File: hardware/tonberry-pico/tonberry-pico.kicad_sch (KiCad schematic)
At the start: 10 parts, among them J1 MicroSD_Breakout, J2 SparkFun I2S Audio Breakout M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, J3 RC522_Breakout, SW1 SW_Push, SW2 SW_Push, SW3 SW_Push, U1 Pico

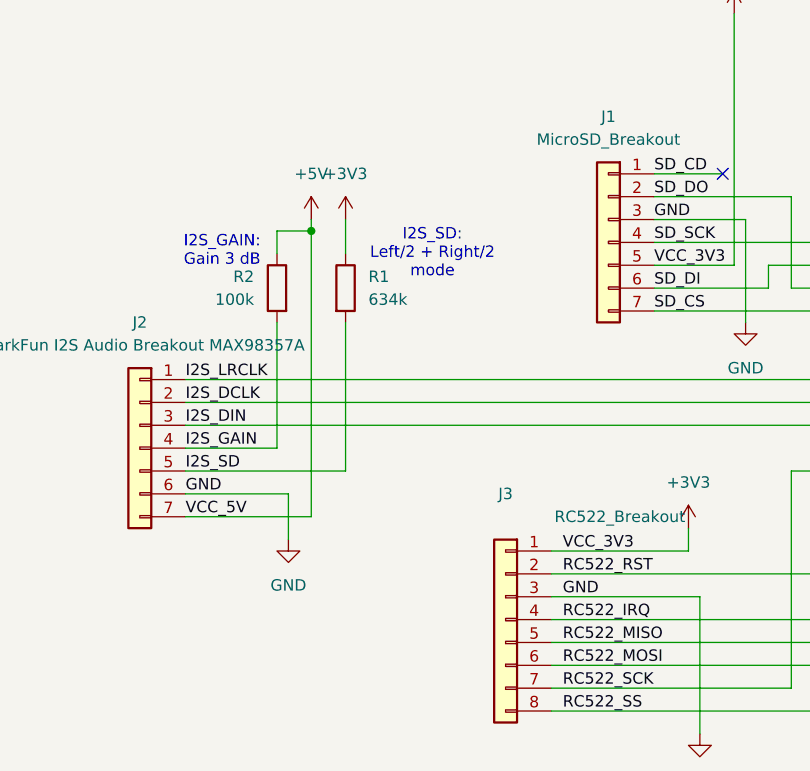
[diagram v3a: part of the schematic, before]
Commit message: schematic: Fix I2S_SD pullup
Sparkfun I2S audio board already has MAX98357A SD pin pullup for mono
mode, so external pullup is redundant and can actually cause issues.
Remove it.
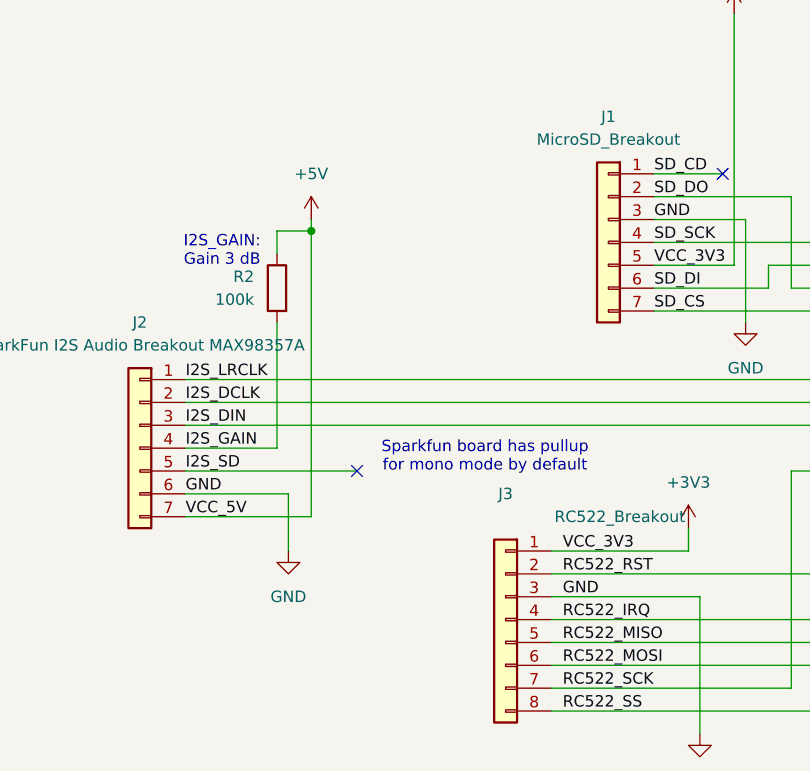
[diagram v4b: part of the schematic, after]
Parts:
- removed R1: 634k, symbol Device:R
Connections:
- no-connect marks 2 -> 3
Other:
- note added: "Sparkfun board has pullup for mono mode by default"
- note removed: "I2S_SD: Left/2 + Right/2 mode"
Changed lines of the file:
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@@
 		)
 	)
-	(text "I2S_SD:\nLeft/2 + Right/2\nmode"
+	(text "Sparkfun board has pullup\nfor mono mode by default"
 		(exclude_from_sim no)
-		(at 59.182 68.58 0)
+		(at 65.024 91.186 0)
 		(effects
 			(font
@@
 	)
 	(no_connect
+		(at 50.8 92.71)
+	)
+	(no_connect
 		(at 170.18 139.7)
 	)
@@
 	(wire
 		(pts
-			(xy 31.75 92.71) (xy 49.53 92.71)
-		)
-		(stroke
-			(width 0)
-			(type default)
-		)
-	)
-	(wire
-		(pts
 			(xy 157.48 59.69) (xy 162.56 59.69)
 		)
@@
 	(wire
 		(pts
+			(xy 31.75 92.71) (xy 50.8 92.71)
+		)
+		(stroke
+			(width 0)
+			(type default)
+		)
+	)
+	(wire
+		(pts
 			(xy 121.92 85.09) (xy 104.14 85.09)
 		)
@@
 	(wire
 		(pts
-			(xy 49.53 76.2) (xy 49.53 92.71)
-		)
-		(stroke
-			(width 0)
-			(type default)
-		)
-	)
-	(wire
-		(pts
 			(xy 99.06 62.23) (xy 99.06 72.39)
 		)
@@
 	(wire
 		(pts
-			(xy 43.18 100.33) (xy 43.18 95.25)
+			(xy 43.18 95.25) (xy 43.18 101.6)
 		)
 		(stroke
@@
 		(pts
 			(xy 72.39 104.14) (xy 109.22 104.14)
-		)
-		(stroke
-			(width 0)
-			(type default)
-		)
-	)
-	(wire
-		(pts
-			(xy 49.53 64.77) (xy 49.53 68.58)
 		)
 		(stroke
@@
 			)
 			(justify left bottom)
-		)
-	)
-	(symbol
-		(lib_id "Device:R")
-		(at 49.53 72.39 0)
-		(unit 1)
-		(exclude_from_sim no)
-		(in_bom yes)
-		(on_board yes)
-		(dnp no)
-		(property "Reference" "R1"
-			(at 52.07 71.1199 0)
-			(effects
-				(font
-					(size 1.27 1.27)
-				)
-				(justify left)
-			)
-		)
-		(property "Value" "634k"
-			(at 52.07 73.6599 0)
-			(effects
-				(font
-					(size 1.27 1.27)
-				)
-				(justify left)
-			)
-		)
-		(property "Footprint" ""
-			(at 47.752 72.39 90)
-			(effects
-				(font
-					(size 1.27 1.27)
-				)
-				(hide yes)
-			)
-		)
-		(property "Datasheet" "~"
-			(at 49.53 72.39 0)
-			(effects
-				(font
-					(size 1.27 1.27)
-				)
-				(hide yes)
-			)
-		)
-		(property "Description" "Resistor"
-			(at 49.53 72.39 0)
-			(effects
-				(font
-					(size 1.27 1.27)
-				)
-				(hide yes)
-			)
-		)
-		(pin "2"
-		)
-		(pin "1"
-		)
-		(instances
-			(project "tonberry-pico"
-				(path "/7226ca0f-138a-46b4-89f3-dc32dfb1f9f7"
-					(reference "R1")
-					(unit 1)
-				)
-			)
-		)
-	)
-	(symbol
-		(lib_id "power:+3V3")
-		(at 49.53 64.77 0)
-		(unit 1)
-		(exclude_from_sim no)
-		(in_bom yes)
-		(on_board yes)
-		(dnp no)
-		(fields_autoplaced yes)
-		(property "Reference" "#PWR07"
-			(at 49.53 68.58 0)
-			(effects
-				(font
-					(size 1.27 1.27)
-				)
-				(hide yes)
-			)
-		)
-		(property "Value" "+3V3"
-			(at 49.53 59.69 0)
-			(effects
-				(font
-					(size 1.27 1.27)
-				)
-			)
-		)
-		(property "Footprint" ""
-			(at 49.53 64.77 0)
-			(effects
-				(font
-					(size 1.27 1.27)
-				)
-				(hide yes)
-			)
-		)
-		(property "Datasheet" ""
-			(at 49.53 64.77 0)
-			(effects
-				(font
-					(size 1.27 1.27)
-				)
-				(hide yes)
-			)
-		)
-		(property "Description" "Power symbol creates a global label with name \"+3V3\""
-			(at 49.53 64.77 0)
-			(effects
-				(font
-					(size 1.27 1.27)
-				)
-				(hide yes)
-			)
-		)
-		(pin "1"
-		)
-		(instances
-			(project "tonberry-pico"
-				(path "/7226ca0f-138a-46b4-89f3-dc32dfb1f9f7"
-					(reference "#PWR07")
-					(unit 1)
-				)
-			)
 		)
 	)
@@
 	(symbol
 		(lib_id "power:GND")
-		(at 43.18 100.33 0)
+		(at 43.18 101.6 0)
 		(unit 1)
 		(exclude_from_sim no)
@@
 		(fields_autoplaced yes)
 		(property "Reference" "#PWR05"
+			(at 43.18 107.95 0)
+			(effects
+				(font
+					(size 1.27 1.27)
+				)
+				(hide yes)
+			)
+		)
+		(property "Value" "GND"
 			(at 43.18 106.68 0)
 			(effects
@@
 					(size 1.27 1.27)
 				)
-				(hide yes)
-			)
-		)
-		(property "Value" "GND"
-			(at 43.18 105.41 0)
-			(effects
-				(font
-					(size 1.27 1.27)
-				)
 			)
 		)
 		(property "Footprint" ""
-			(at 43.18 100.33 0)
+			(at 43.18 101.6 0)
 			(effects
 				(font
@@
 		)
 		(property "Datasheet" ""
-			(at 43.18 100.33 0)
+			(at 43.18 101.6 0)
 			(effects
 				(font
@@
 		)
 		(property "Description" "Power symbol creates a global label with name \"GND\" , ground"
-			(at 43.18 100.33 0)
-			(effects
-				(font
+			(at 43.18 101.6 0)
+			(effects
+				(font

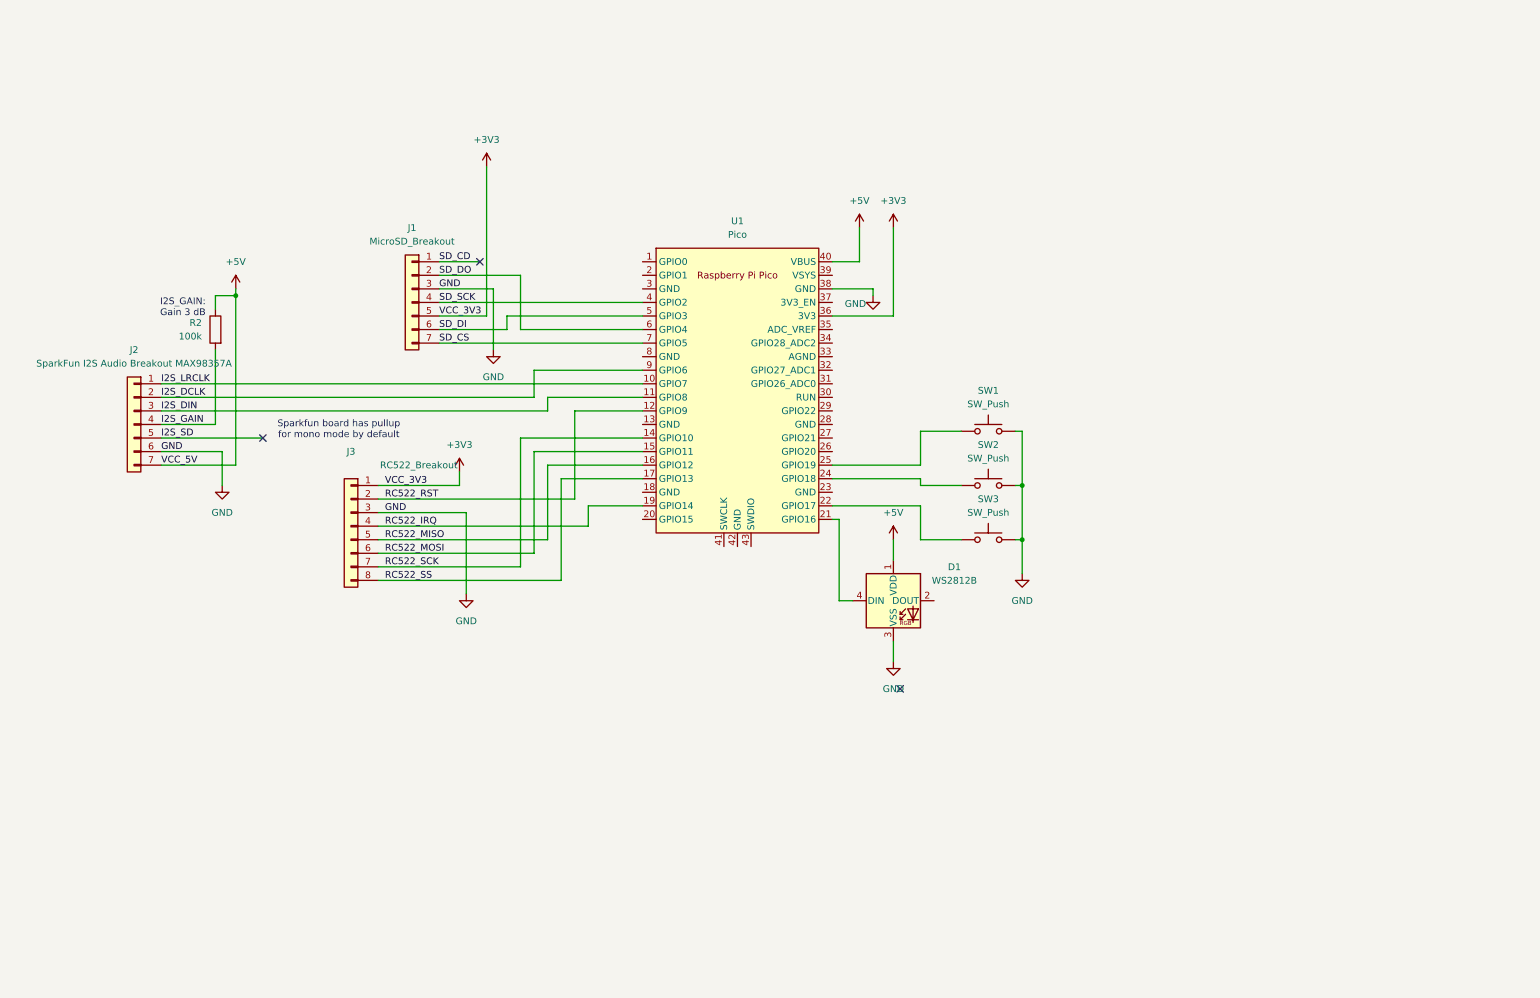
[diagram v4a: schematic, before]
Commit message: Add battery charger, PCB rev 1
Signed-off-by: Matthias Blankertz <matthias@blankertz.org>
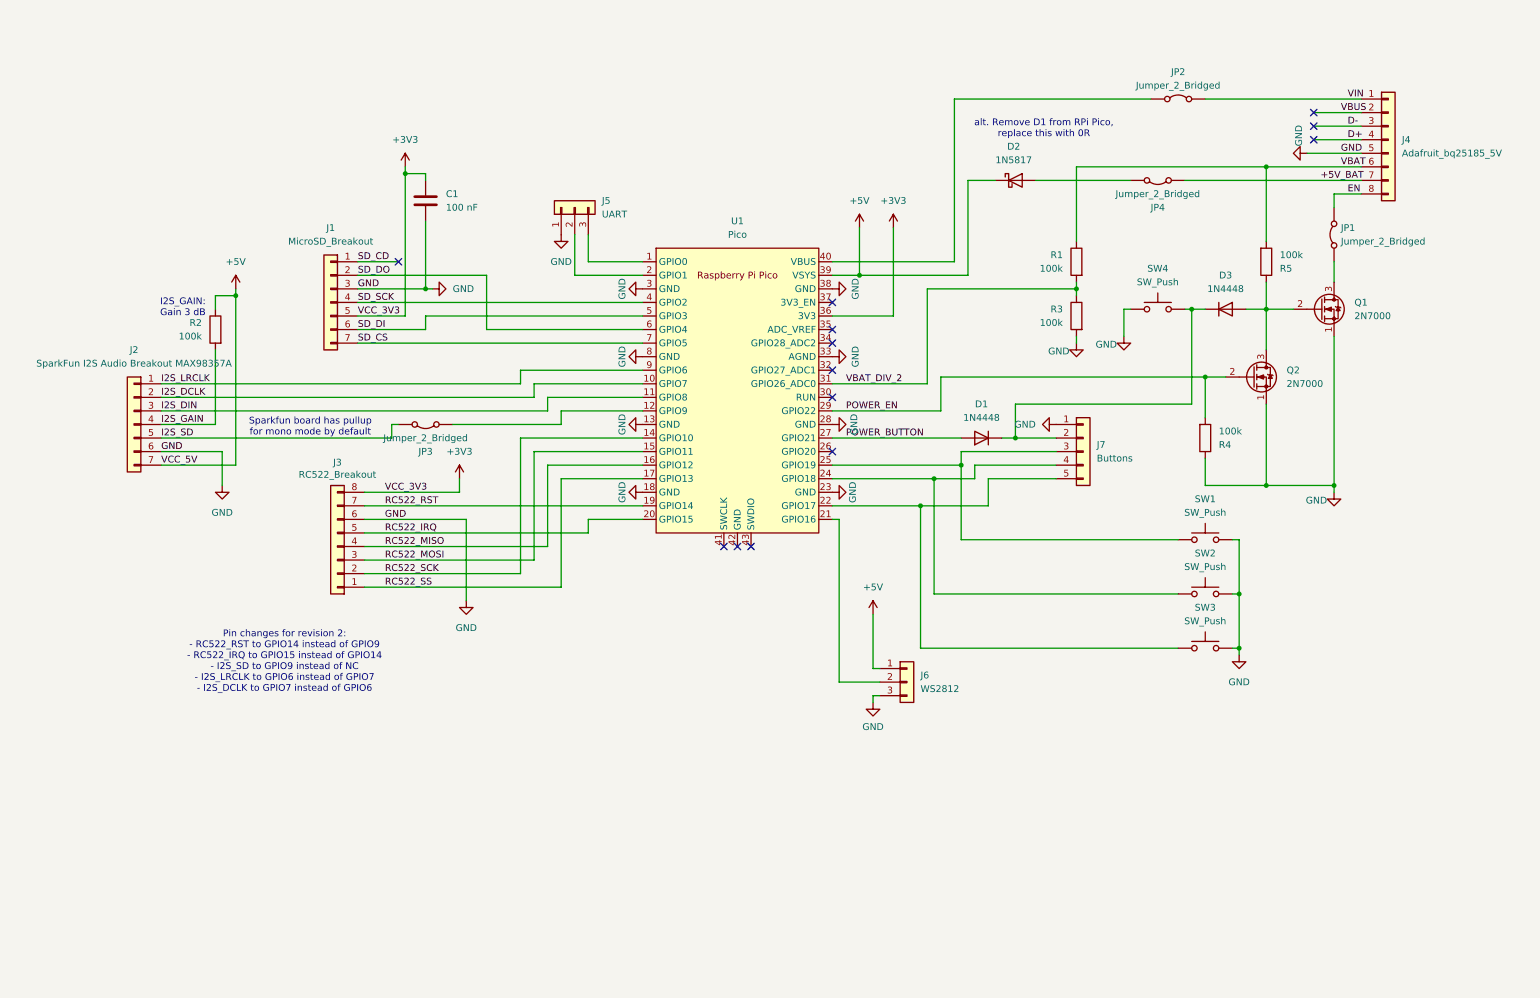
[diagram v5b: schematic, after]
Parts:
- removed D1: WS2812B, LED_SMD:LED_WS2812B_PLCC4_5.0x5.0mm_P3.2mm, symbol LED:WS2812B
- added C1: 100 nF, Capacitor_THT:C_Disc_D5.0mm_W2.5mm_P5.00mm, symbol Device:C
- added D1, D3: 1N4448, Diode_THT:D_DO-35_SOD27_P7.62mm_Horizontal, symbol Device:D
- added D2: 1N5817, Diode_THT:D_DO-41_SOD81_P10.16mm_Horizontal, symbol Device:D_Schottky
- added J4: Adafruit_bq25185_5V, Modules:Adafruit_bq25185, symbol Connector_Generic:Conn_01x08
- added J5: UART, Connector_PinHeader_2.54mm:PinHeader_1x03_P2.54mm_Vertical, symbol Connector_Generic:Conn_01x03
- added J6: WS2812, Connector_PinSocket_2.54mm:PinSocket_1x03_P2.54mm_Vertical, symbol Connector_Generic:Conn_01x03
- added J7: Buttons, Connector_PinSocket_2.54mm:PinSocket_1x05_P2.54mm_Vertical, symbol Connector_Generic:Conn_01x05
- added JP1, JP2, JP3, JP4: Jumper_2_Bridged, Connector_PinHeader_2.54mm:PinHeader_1x02_P2.54mm_Vertical, symbol Jumper:Jumper_2_Bridged
- added Q1, Q2: 2N7000, Package_TO_SOT_THT:TO-92_Inline, symbol Transistor_FET:2N7000
- added R1, R3, R4, R5: 100k, Resistor_THT:R_Axial_DIN0207_L6.3mm_D2.5mm_P10.16mm_Horizontal, symbol Device:R
- added SW4: SW_Push, Button_Switch_THT:Push_E-Switch_KS01Q01, symbol Switch:SW_Push
- J1: footprint (none) -> Modules:Sparkfun_MicroSD_Breakout
- J2: footprint (none) -> Modules:Sparkfun_MAX98357A
- J3: footprint (none) -> Modules:AZ_Delivery_RC522
- R2: footprint (none) -> Resistor_THT:R_Axial_DIN0207_L6.3mm_D2.5mm_P10.16mm_Horizontal
- SW1, SW2, SW3: footprint (none) -> Button_Switch_THT:Push_E-Switch_KS01Q01
- U1: footprint RPi_Pico:RPi_Pico_SMD_TH -> Module:RaspberryPi_Pico_Common_THT
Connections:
- net +3V3: now also J3.8 (Pin_8), C1.1; no longer J3.1 (Pin_1)
- net +5V: now also U1.39 (VSYS), D2.1 (K), J6.1 (Pin_1); no longer U1.40 (VBUS)
- net GND: now also J3.6 (Pin_6), U1.13 (GND), U1.18 (GND), U1.23 (GND), U1.28 (GND), U1.3 (GND), U1.33 (AGND), U1.8 (GND), C1.2, J4.5 (Pin_5), J5.1 (Pin_1), J6.3 (Pin_3), J7.1 (Pin_1), Q1.1 (S), Q2.1 (S), R3.2, R4.1, SW4.2; no longer J3.3 (Pin_3)
- net I2S_DCLK: now also U1.10 (GPIO7); no longer U1.9 (GPIO6)
- net I2S_LRCLK: now also U1.9 (GPIO6); no longer U1.10 (GPIO7)
- net I2S_SD: now also JP3.1 (A)
- net RC522_IRQ: now also J3.5 (Pin_5), U1.20 (GPIO15); no longer J3.4 (Pin_4), U1.19 (GPIO14)
- net RC522_MISO: now also J3.4 (Pin_4); no longer J3.5 (Pin_5)
- net RC522_MOSI: now also J3.3 (Pin_3); no longer J3.6 (Pin_6)
- net RC522_RST: now also J3.7 (Pin_7), U1.19 (GPIO14); no longer J3.2 (Pin_2), U1.12 (GPIO9)
- net RC522_SCK: now also J3.2 (Pin_2); no longer J3.7 (Pin_7)
- net RC522_SS: now also J3.1 (Pin_1); no longer J3.8 (Pin_8)
- net at SW3.1, U1.22 (GPIO17): now also J7.5 (Pin_5)
- net at U1.1 (GPIO0): now also J5.3 (Pin_3)
- net at U1.2 (GPIO1): now also J5.2 (Pin_2)
- net at U1.21 (GPIO16): now also J6.2 (Pin_2)
- net at SW2.1, U1.24 (GPIO18): now also J7.4 (Pin_4)
- net at SW1.1, U1.25 (GPIO19): now also J7.3 (Pin_3)
- net POWER_BUTTON: now reaches U1.27 (GPIO21)
- net POWER_BUTTON: now also D1.2 (A)
- net POWER_EN: now reaches U1.29 (GPIO22)
- net POWER_EN: now also Q2.2 (G), R4.2
- net VBAT_DIV_2: now reaches U1.31 (GPIO26_ADC0)
- net VBAT_DIV_2: now also R1.2, R3.1
- new net: JP3.2 (B), U1.12 (GPIO9)
- new net: D3.2 (A), Q1.2 (G), Q2.3 (D), R5.1
- new net: D1.1 (K), D3.1 (K), J7.2 (Pin_2), SW4.1
- new net: JP2.1 (A), U1.40 (VBUS)
- new net: D2.2 (A), JP4.1 (A)
- new net: JP1.1 (A), Q1.3 (D)
- new net +5V_BAT: J4.7 (Pin_7), JP4.2 (B)
- new net D+: J4.4 (Pin_4)
- new net D-: J4.3 (Pin_3)
- new net EN: J4.8 (Pin_8), JP1.2 (B)
- new net VBAT: J4.6 (Pin_6), R1.1, R5.2
- new net VBUS: J4.2 (Pin_2)
- new net VIN: J4.1 (Pin_1), JP2.2 (B)
- no-connect marks 3 -> 13
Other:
- note added: "Pin changes for revision 2: - RC522_RST to GPIO14 instead of GPIO9 - RC522_IRQ to GPIO15 instead of GPIO14 - I2S_SD to GPIO9 instead of NC - I2S_LRCLK to GPIO6 instead of GPIO7 - I2S_DCLK to GPIO7 instead of GPIO6"
- note added: "alt. Remove D1 from RPi Pico, replace this with 0R"
- moved on the sheet: J1, J3, SW1, SW2, SW3

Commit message: hw: Clean up schematic, add RUN reset
Clean up schematic and put battery power, buttons and run/reset in
subblocks.

Add missing switch on RUN to reset the RP2040. In the PCB this is
actually a jumper instead of a switch right now, so it fits in the
existing layout.

Signed-off-by: Matthias Blankertz <matthias@blankertz.org>
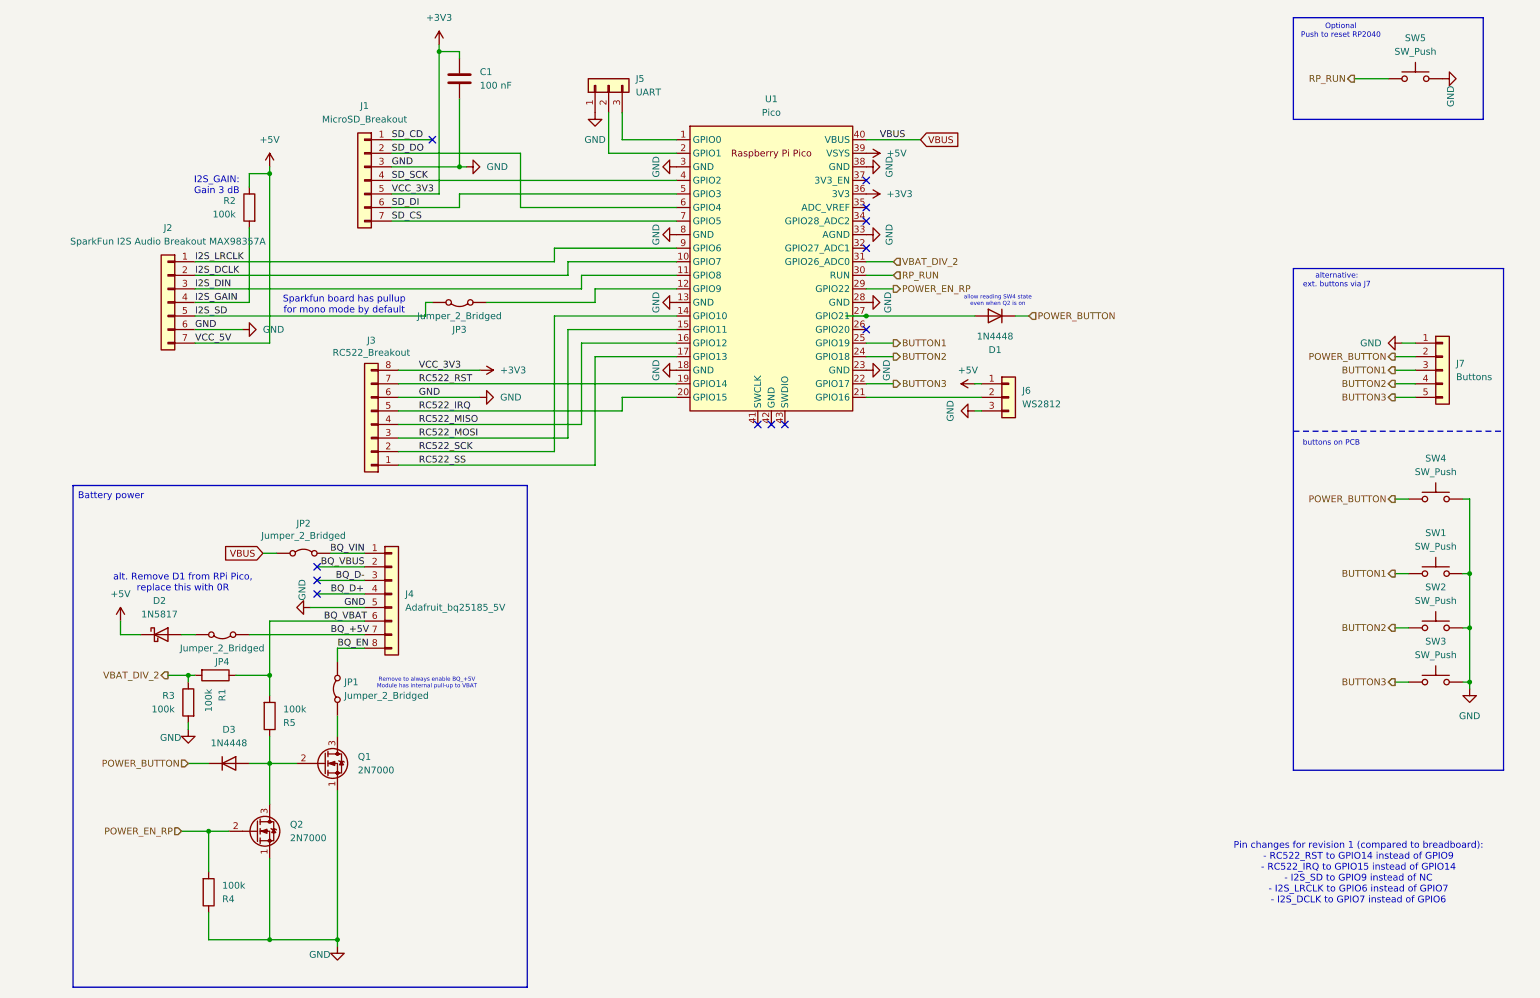
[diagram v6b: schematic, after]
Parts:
- added SW5: SW_Push, Button_Switch_THT:Push_E-Switch_KS01Q01, symbol Switch:SW_Push
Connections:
- net GND: now also SW5.1
- net POWER_BUTTON: now also D1.1 (K), D3.1 (K), J7.2 (Pin_2), SW4.1; no longer D1.2 (A), U1.27 (GPIO21)
- net VBUS: now also JP2.1 (A), U1.40 (VBUS); no longer J4.2 (Pin_2)
- net BUTTON3: now reaches J7.5 (Pin_5), SW3.1, U1.22 (GPIO17)
- net BUTTON2: now reaches J7.4 (Pin_4), SW2.1, U1.24 (GPIO18)
- net BUTTON1: now reaches J7.3 (Pin_3), SW1.1, U1.25 (GPIO19)
- net RP_RUN: now reaches U1.30 (RUN)
- net RP_RUN: now also SW5.2
- net +5V_BAT renamed BQ_+5V
- net D+ renamed BQ_D+
- net D- renamed BQ_D-
- net EN renamed BQ_EN
- net POWER_EN renamed POWER_EN_RP
- net VBAT renamed BQ_VBAT
- net VIN renamed BQ_VIN
- new net: D1.2 (A), U1.27 (GPIO21)
- new net BQ_VBUS: J4.2 (Pin_2)
- no-connect marks 13 -> 12
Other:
- note added: "Battery power"
- note added: "Optional Push to reset RP2040"
- note added: "Pin changes for revision 1 (compared to breadboard): - RC522_RST to GPIO14 instead of GPIO9 - RC522_IRQ to GPIO15 instead of GPIO14 - I2S_SD to GPIO9 instead of NC - I2S_LRCLK to GPIO6 instead of GPIO7 - I2S_DCLK to GPIO7 instead of GPIO6"
- note added: "Remove to always enable BQ_+5V Module has internal pull-up to VBAT"
- note added: "allow reading SW4 state even when Q2 is on"
- note added: "alternative: ext. buttons via J7"
- note added: "buttons on PCB"
- note removed: "Pin changes for revision 2: - RC522_RST to GPIO14 instead of GPIO9 - RC522_IRQ to GPIO15 instead of GPIO14 - I2S_SD to GPIO9 instead of NC - I2S_LRCLK to GPIO6 instead of GPIO7 - I2S_DCLK to GPIO7 instead of GPIO6"
- moved on the sheet: C1, D1, D2, D3, J1, J2, J3, J4, J5, J6, J7, JP1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
